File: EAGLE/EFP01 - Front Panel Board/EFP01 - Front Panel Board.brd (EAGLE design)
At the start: 100 x 86.6 mm, 109 parts, among them J20 Intel EDISON, J21 PWRBUTTON, J22 SERIAL CONS., J23 B14B-PH, J3 USB-A, J4 101-00581-59, J9 ESTOP, Q2 25MHz, U10 FT231XS-R, U11 74LVC1T45, U12 74LVC1T45, U13 74LVC1T45, U14 74LVC1T45, U15 74LVC1T45, U16 TXS0206-29, U17 74LVC, U18 MIC2026-1YM, U19 MIC2026-1YM, U20 74LVC, U21 74LVC1T45, U22 74LVC1T45, U3 93LC66A, U4 LAN9514, U9 SP3485

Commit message: Finalized schematics (minus potential LDO regulator) for all boards. Layout partially done for EFD01
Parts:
- removed C36: 220uF, TinWhiskers:C-SMD-10MM
- removed C50: 470uF, TinWhiskers:C-SMD-10MM
- removed FID4, FID5, FID6: FIDUCIAL, FirePick:FIDUCIAL
- removed J21: PWRBUTTON, TinWhiskers:CON-HDR-2POS-MALE
- removed J22: SERIAL CONS., TinWhiskers:CON-HDR-4POS-MALE
- removed J23: B14B-PH, TinWhiskers:CONN-JST-PH-2.0MM-14P-VRT
- removed J9: ESTOP, TinWhiskers:CON-HDR-2POS-MALE
- removed L2: 100uH, TinWhiskers:L-SMD-12.5MM
- added C1: 220uF, TinWhiskers:C-SMD-6.3MM
- added C3: 470uF, TinWhiskers:C-SMD-6.3MM
- added J1: PWRBTN, TinWhiskers:CONN-JST-PH-2.0MM-4P-SMT-RA
- added J16, J17, J6: S8B-PH-SM4, TinWhiskers:CONN-JST-PH-2.0MM-8P-SMT-RA
- added J18: S6B-PH-SM4, TinWhiskers:CONN-JST-PH-2.0MM-6P-SMT-RA
- added J2: ESTOP, TinWhiskers:CONN-JST-PH-2.0MM-2P-SMT-RA
- added J5: LCD, TinWhiskers:CON-HDR-34POS(2R)-MALE
- added J7: USB-B, TinWhiskers:USB-B(SMT)-VERT-1734517
- added L1: 100uH, TinWhiskers:2020
- added R1: 4.7K, TinWhiskers:R0603
- added R2: 10K, TinWhiskers:R0603
- added R3: ORNG, TinWhiskers:R0603
- added TB1: DCIN, TinWhiskers:TBLOCK-3-5MM-OSTTH030160
- added U1, U2, U23, U24, U25, U26, U27, U28, U30, U5, U6, U7, U8: 74LVC1T45, TinWhiskers:SOT-363
- J3: value USB-A -> USB-A(2.0); device TinWhiskers:CON-HDR-4POS-MALE -> TinWhiskers:USB-A-THRU-VERT-2.0
- U17, U20: value 74LVC -> OR
- moved J3 293.8 mm to (-11.4, -223.1), turned to 0 degrees
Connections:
- removed net ESTOP_OE: J9.2
- new net !ENBL_MOD: J16.2, J17.2, J18.2, J6.2
- new net +24V: J16.1, J17.1, J18.1, J6.1, R3.2, TB1.1
- new net 74DIR: J20.25, U30.3
- new net 74DIRO: U1.5, U2.5, U23.5, U24.5, U25.5, U26.5, U27.5, U28.5, U30.4, U5.5, U6.5, U7.5, U8.5
- new net D0O: J20.52, U24.4
- new net D1O: J20.54, U23.4
- new net D2O: J20.50, U7.4
- new net D3O: J20.56, U8.4
- new net D4O: J20.24, U6.4
- new net D5O: J20.26, U5.4
- new net D6O: J20.28, U1.4
- new net D7O: J20.30, U2.4
- new net ESTOPIN: J2.1, R2.1
- new net LCD_BL: J5.23
- new net LCD_CLK: J5.34
- new net LCD_D10: J5.16
- new net LCD_D11: J5.17
- new net LCD_D12: J5.18
- new net LCD_D13: J5.19
- new net LCD_D14: J5.20
- new net LCD_D15: J5.21
- new net LCD_D8: J5.14
- new net LCD_D9: J5.15
- new net LCD_FCS: J5.32
- new net LCD_MISO: J5.29
- new net LCD_MOSI: J5.30
- new net LCD_PEN: J5.31
- new net LCD_RST: J5.5
- new net LCD_SDCS: J5.22
- new net LCD_TCS: J5.33
- new net LCSO: J20.39, U25.4
- new net LRDO: J20.37, U27.4
- new net LRSO: J20.34, U28.4
- new net LWRO: J20.32, U26.4
- new net N$10: J2.2, R1.2
- new net NC: J5.28
- new net VDD: J5.24, J5.25
- net !PWRBTN: now also J1.1; no longer J21.1
- net +1V8: now also U1.1, U2.6, U23.1, U24.1, U25.6, U26.6, U27.6, U28.6, U30.6, U5.1, U6.1, U7.1, U8.6
- net +3V3: now also C3.POS, L1.2, R2.2, U1.6, U2.1, U23.6, U24.6, U25.1, U26.1, U27.1, U28.1, U30.1, U5.6, U6.6, U7.6, U8.1; no longer C50.POS, J23.1, L2.P$2
- net +5V: now also C1.POS, J18.6, J6.6, TB1.2; no longer C36.POS
- net A: now also J16.4, J17.4, J18.4, J6.4
- net B: now also J16.5, J17.5, J18.5, J6.5
- net DM: now also J7.3; no longer J22.3
- net DP: now also J7.2; no longer J22.2
- net EE_D+: now also J16.7
- net EE_D-: now also J16.8
- net GND: now also C1.NEG, C3.NEG, J1.2, J1.4, J16.3, J17.3, J18.3, J5.26, J5.27, J6.3, J7.4, R1.1, TB1.3, U1.2, U2.2, U23.2, U24.2, U25.2, U26.2, U27.2, U28.2, U30.2, U30.5, U5.2, U6.2, U7.2, U8.2; no longer C36.NEG, C50.NEG, J21.2, J22.4, J23.2
- net LCD_CS: now also J5.1, U25.3; no longer J20.39, J23.11
- net LCD_D0: now also J5.6, U24.3; no longer J20.52, J23.3
- net LCD_D1: now also J5.7, U23.3; no longer J20.54, J23.4
- net LCD_D2: now also J5.8, U7.3; no longer J20.50, J23.5
- net LCD_D3: now also J5.9, U8.3; no longer J20.56, J23.6
- net LCD_D4: now also J5.10, U6.3; no longer J20.24, J23.7
- net LCD_D5: now also J5.11, U5.3; no longer J20.26, J23.8
- net LCD_D6: now also J5.12, U1.3; no longer J20.28, J23.9
- net LCD_D7: now also J5.13, U2.3; no longer J20.30, J23.10
- net LCD_RD: now also J5.4, U27.3; no longer J20.37, J23.14
- net LCD_RS: now also J5.2, U28.3; no longer J20.34, J23.12
- net LCD_WR: now also J5.3, U26.3; no longer J20.32, J23.13
- net N$16: now also L1.1; no longer L2.P$1
- net N$2: now also J7.1; no longer J22.1
- net N$5: now also J1.3, R3.1; no longer J9.1
- net PWR1: now also J16.6
- net PWR2: now also J17.6
- net ULC_D+: now also J17.7
- net ULC_D-: now also J17.8
- net USBMCU+: now also J6.7
- net USBMCU-: now also J6.8

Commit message: Routed all boards. EFP01 has a serious problem with spacing. Even on minimum allowable there are 300 DRC errors.
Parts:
- removed C1: 220uF, TinWhiskers:C-SMD-6.3MM
- removed C33, C34, C35: 0.1uF, TinWhiskers:C0603
- removed C51: 0.47uF, TinWhiskers:C0603
- removed D15: SJPB-H6, TinWhiskers:DIO-SM2
- removed J4: 101-00581-59, TinWhiskers:MICRO-SD-SOCKET-AMPH
- removed L1: 100uH, TinWhiskers:2020
- removed R17, R23: 10.5K, TinWhiskers:R0603
- removed U16: TXS0206-29, TinWhiskers:20-XFBGA
- removed VR2: SI-8033JD, TinWhiskers:TO263-5
- added C4: 10uF, TinWhiskers:C-SMD-6.3MM
- added VR1: LMS8117AMP-3.3/NOPB, TinWhiskers:SOT-223
- C3: value 470uF -> 10uF
- J5: device TinWhiskers:CON-HDR-34POS(2R)-MALE -> TinWhiskers:LCD-34P-3.2IN
- moved J3 318.3 mm to (197.1, 17.3), turned to 90 degrees
- moved U30 303.1 mm to (163.4, 67.1), flipped to the bottom, turned to 270 degrees
- moved J7 301.0 mm to (132.6, 62.0), flipped to the bottom
- moved J6 237.6 mm to (127.2, 7.98), flipped to the bottom, turned to 180 degrees
- moved C3 229.1 mm to (29.7, 12.9), flipped to the bottom, turned to 180 degrees
- moved U28 198.1 mm to (50.6, 14.8), flipped to the bottom, turned to 270 degrees
- moved U27 195.3 mm to (50.7, 17.8), flipped to the bottom, turned to 270 degrees
- moved U26 193.1 mm to (64.5, 17.3), flipped to the bottom
- moved U25 184.0 mm to (64.5, 13.7), flipped to the bottom
- moved U23 181.9 mm to (64.6, 23.3), flipped to the bottom
- moved U24 181.2 mm to (50.7, 21.1), flipped to the bottom, turned to 270 degrees
- moved U8 179.5 mm to (64.5, 26.7), flipped to the bottom
- moved U7 167.1 mm to (50.7, 24.3), flipped to the bottom, turned to 270 degrees
- moved J2 166.4 mm to (69.0, 61.6), flipped to the bottom
- moved U5 166.1 mm to (64.5, 30.2), flipped to the bottom
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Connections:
- removed net CLKA: J20.58, U16.D2
- removed net CLKB: J4.5, U16.D3
- removed net CLKF: J20.44, U16.E2
- removed net CMD: J4.3
- removed net CMDA: J20.62, U16.C1
- removed net CMDB: U16.C4
- removed net DAT0A: J20.66, U16.D1
- removed net DAT0B: J4.7, U16.D4
- removed net DAT1A: J20.70, U16.E1
- removed net DAT1B: J4.8, U16.E4
- removed net DAT2: J4.1
- removed net DAT2A: J20.64, U16.A1
- removed net DAT2B: U16.A4
- removed net DAT3: J4.2
- removed net DAT3A: J20.68, U16.B1
- removed net DAT3B: U16.B4
- removed net EN: R17.1, U16.E3
- removed net N$16: D15.POS, L1.1, VR2.2
- removed net N$17: C51.2, VR2.5
- removed net SD_CD: J20.60, J4.CD, R23.1, U16.A3
- removed net VCCB: C34.2, J4.4, U16.B3
- new net RESET: U10.14
- net !RXLED: now also U10.10
- net !TXLED: now also U10.17
- net +1V8: no longer C35.2, R17.2, R23.2, U16.A2
- net +3V3: now also C4.POS, U10.3, VR1.2; no longer C3.POS, C33.2, L1.2, U16.B2, VR2.4
- net +5V: now also C3.POS, VR1.3; no longer C1.POS, VR2.1
- net DM: now also U10.12
- net DP: now also U10.11
- net GND: now also C4.NEG, RJ1.8, U10.16, U10.6, VR1.1, VR1.P$1; no longer C1.NEG, C33.1, C34.1, C35.1, C51.1, D15.NEG, J4.6, J4.GND, J4.GND2, J4.NC, U16.C2, U16.C3, VR2.3, VR2.GND
- net N$1: now also U10.13
- net RXD: now also U10.4
- net TXDO: now also U10.20
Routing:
- net +3V3: track 0.00 -> 583.4 mm, vias 0 -> 34
- net +5V: track 0.00 -> 323.3 mm, vias 0 -> 5
- net GND: track 0.00 -> 308.2 mm, vias 0 -> 88
- net +1V8: track 0.00 -> 284.1 mm, vias 0 -> 26
- net 74DIRO: track 0.00 -> 229.8 mm, vias 0 -> 14
- net LRSO: track 0.00 -> 198.0 mm, vias 0 -> 8
- net D0O: track 0.00 -> 182.0 mm, vias 0 -> 4
- net LRDO: track 0.00 -> 180.1 mm, vias 0 -> 2
- net D2O: track 0.00 -> 174.3 mm, vias 0 -> 4
- net LCSO: track 0.00 -> 169.4 mm, vias 0 -> 6
- net B: track 0.00 -> 163.0 mm, vias 0 -> 7
- net D1O: track 0.00 -> 162.5 mm, vias 0 -> 2
- net D4O: track 0.00 -> 161.9 mm, vias 0 -> 4
- net D3O: track 0.00 -> 158.6 mm, vias 0 -> 2
- net LWRO: track 0.00 -> 158.6 mm, vias 0 -> 2
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- added copper zone on layer 15, net +24V
- added copper zone on layer 2, net GND
- removed copper zone on layer 1, net GND
- removed copper zone on layer 16, net GND
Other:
- board size 100 x 86.6 mm -> 200 x 69.6 mm
- board text removed: "ENCODER"
- board text removed: "ENDSTOP"
- board text removed: "MOT"
- board text removed: "RXD"
- board text removed: "X AXIS"
- board text removed: "Y AXIS"

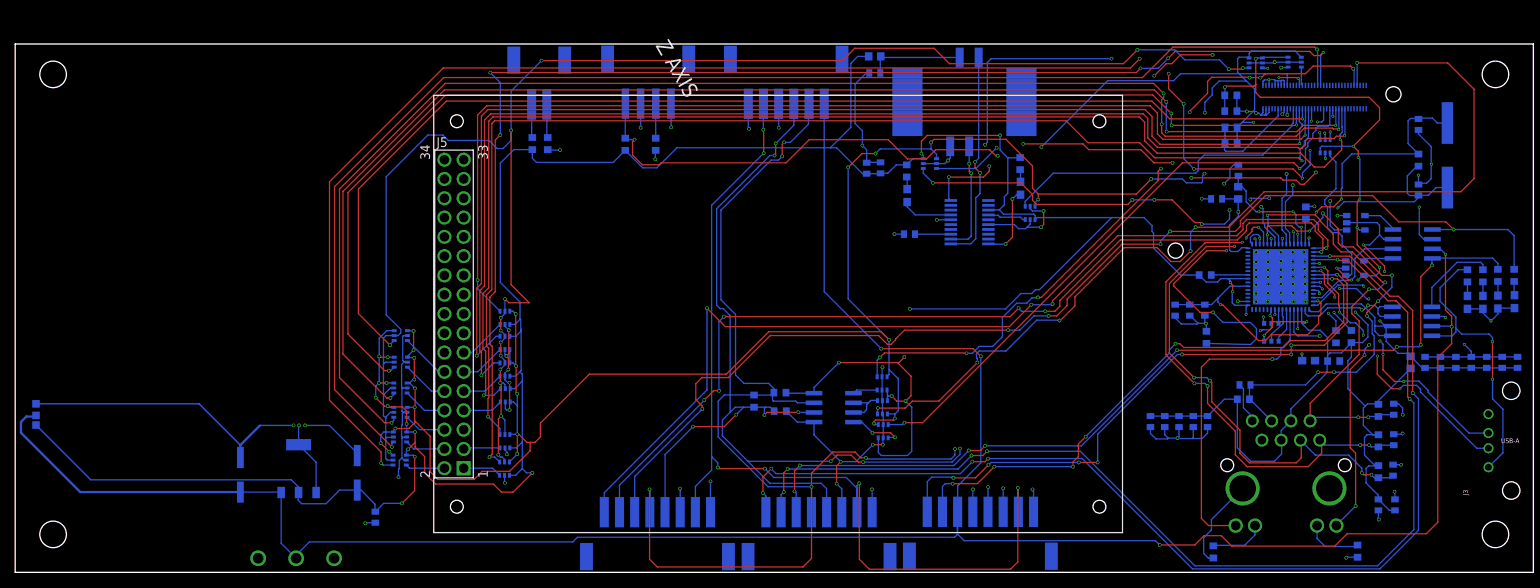
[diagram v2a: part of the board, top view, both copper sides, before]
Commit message: Completed boards. Please look at airwires connecting thermal pads to GND vias. They shouldn't be present due to the vias.
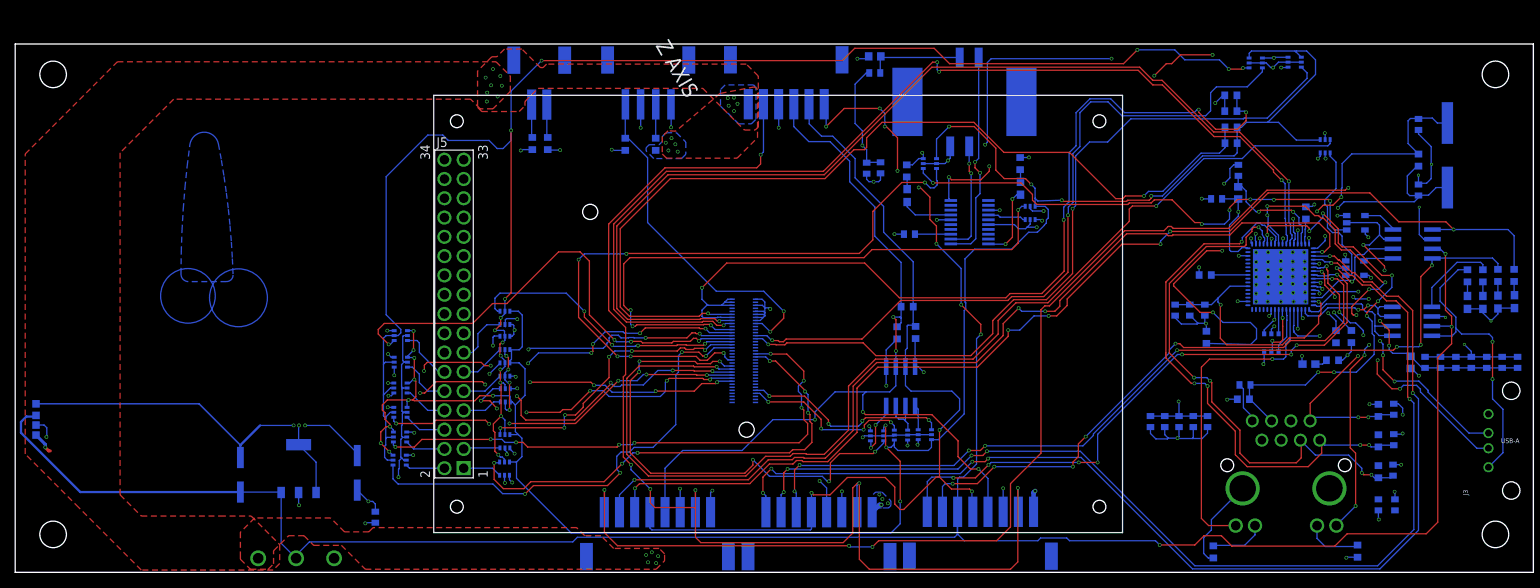
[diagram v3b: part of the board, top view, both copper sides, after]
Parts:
- added TP3: +5V, TinWhiskers:TESTPAD
- J1: device TinWhiskers:CONN-JST-PH-2.0MM-4P-SMT-RA -> TinWhiskers:CON-JST-PH-2.0MM-4P-SMT-RA
- J2: device TinWhiskers:CONN-JST-PH-2.0MM-2P-SMT-RA -> TinWhiskers:CON-JST-PH-2.0MM-2P-SMT-RA
- moved J20 82.3 mm to (96.0, 29.2), turned to 270 degrees
- moved R51 23.7 mm to (117.5, 35.0), turned to 180 degrees
- moved R49 19.6 mm to (118.6, 31.6), turned to 270 degrees
- moved R50 18.5 mm to (116.2, 31.5), turned to 90 degrees
- moved U9 9.24 mm to (116.6, 24.5), turned to 90 degrees
- moved U15 8.80 mm to (119.8, 18.1), turned to 90 degrees
- moved U14 4.40 mm to (116.7, 18.1), turned to 90 degrees
- moved U3 1.37 mm to (165.5, 30.3)
- moved U13 1.02 mm to (113.5, 18.0), turned to 270 degrees
- moved LED11 0.46 mm to (170.4, 27.4)
- moved R10 0.18 mm to (173.5, 27.9), turned to 180 degrees
- moved J1 0.10 mm to (83.4, 61.6)
- moved J18 0.05 mm to (101.6, 61.7)
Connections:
- net +24V: now also TP3.PAD
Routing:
- net +3V3: track 583.4 -> 76.5 mm, vias 34 -> 41
- net EEEN: track 4.47 -> 142.7 mm
- net LRSO: track 198.0 -> 62.8 mm, vias 8 -> 4
- net D0O: track 182.0 -> 48.3 mm, vias 4 -> 6
- net D3O: track 158.6 -> 35.6 mm, vias 2 -> 5
- net USBDM0: track 18.4 -> 140.9 mm, vias 2 -> 4
- net D1O: track 162.5 -> 40.7 mm, vias 2 -> 6
- net D2O: track 174.3 -> 53.5 mm, vias 4 -> 7
- net USBDP0: track 19.1 -> 138.9 mm
- net LWRO: track 158.6 -> 39.2 mm, vias 2 -> 6
- net D5O: track 152.4 -> 35.6 mm, vias 2 -> 4
- net D4O: track 161.9 -> 49.9 mm, vias 4 -> 8
- net N$21: track 8.97 -> 118.7 mm, vias 2 -> 4
- net N$19: track 13.0 -> 121.6 mm, vias 0 -> 2
- net LRDO: track 180.1 -> 73.1 mm, vias 2 -> 8
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- added copper zone on layer 1, net +24V
- added copper zone on layer 16, net +24V
- added copper zone on layer 15, net +3V3
- added copper zone on layer 16, net N$4

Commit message: Updated all boards to include changes for production
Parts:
- added C1, C10, C15, C16, C17, C27, C28, C29, C33, C34, C35, C36, C37, C38, C39, C40, C41, C42, C43, C44, C45, C46, C47, C48, C49, C5, C6, C7, C8, C9: 0.1uF, TinWhiskers:C0603
- added LOGO1, LOGO2: LOGO-FIREPICKLARGE, FirePick:LOGO-FIREPICK
- J16, J17, J6: device TinWhiskers:CONN-JST-PH-2.0MM-8P-SMT-RA -> TinWhiskers:CON-JST-PH-2.0MM-8P-SMT-VRT
- J18: device TinWhiskers:CONN-JST-PH-2.0MM-6P-SMT-RA -> TinWhiskers:CON-JST-PH-2.00MM-6P-SMT-VRT
- moved C11 16.8 mm to (168.8, 54.1), turned to 0 degrees
- moved Q2 16.1 mm to (172.8, 57.9), turned to 180 degrees
- moved R11 11.4 mm to (173.5, 54.1), turned to 180 degrees
- moved C12 8.30 mm to (177.4, 54.1), turned to 180 degrees
- moved C4 6.84 mm to (39.9, 17.6)
- moved VR1 6.65 mm to (32.5, 18.2)
- moved C3 6.61 mm to (24.9, 17.4)
- moved U22 6.61 mm to (174.0, 62.6), turned to 90 degrees
- moved U21 5.44 mm to (120.8, 48.4)
- moved U30 5.04 mm to (163.7, 62.1)
- moved C60 5.04 mm to (114.2, 48.3)
- moved C77 5.04 mm to (118.1, 39.5)
- moved C78 5.04 mm to (113.5, 60.8)
- moved J1 5.04 mm to (83.6, 56.6)
- moved LED9 5.04 mm to (132.7, 45.6)
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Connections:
- net +3V3: now also C1.2, C10.2, C15.2, C16.2, C17.2, C27.2, C28.2, C29.2, C33.2, C34.2, C35.2, C36.2, C37.2, C38.2, C39.2, C40.2, C41.2, C42.2, C43.2, C44.2, C45.2, C46.2, C47.2, C48.2, C49.2, C5.2, C6.2, C7.2, C8.2, C9.2, VR1.P$1; no longer VR1.2
- net GND: now also C1.1, C10.1, C15.1, C16.1, C17.1, C27.1, C28.1, C29.1, C33.1, C34.1, C35.1, C36.1, C37.1, C38.1, C39.1, C40.1, C41.1, C42.1, C43.1, C44.1, C45.1, C46.1, C47.1, C48.1, C49.1, C5.1, C6.1, C7.1, C8.1, C9.1; no longer VR1.P$1
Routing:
- net +3V3: track 76.5 -> 198.1 mm, vias 41 -> 60
- net GND: track 292.0 -> 349.4 mm, vias 87 -> 107
- net EEENO: track 19.7 -> 53.4 mm
- net XO: track 36.7 -> 25.7 mm, vias 3 -> 2
- net +1V8: track 282.4 -> 272.5 mm, vias 16 -> 23
- net N$21: track 118.7 -> 109.4 mm
- net B: track 123.3 -> 131.2 mm, vias 3 -> 5
- net +24V: track 11.6 -> 4.66 mm, vias 30 -> 36
- net TXD: track 100.6 -> 94.4 mm
- net !PWRBTN: track 45.8 -> 40.7 mm
- net 74DIRO: track 227.7 -> 223.2 mm
- net USBA_D-: track 39.0 -> 42.9 mm, vias 5 -> 6
- net USBA_D+: track 35.3 -> 39.3 mm, vias 5 -> 6
- net RD-: track 61.2 -> 65.1 mm
- net !ENBL_MOD: track 163.2 -> 167.1 mm, vias 6 -> 7
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- removed copper zone on layer 16, net N$4
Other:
- board size 200 x 69.6 mm -> 200 x 65 mm
- board text added: "E-STOP"
- board text added: "EMC03"
- board text added: "END EFFECTOR"
- board text added: "ETHERNET"
- board text added: "LCD"
- board text added: "MOD TOOL"
- board text added: "PWR"
- board text added: "PWR BTN"
- board text added: "SBC"
- board text added: "UP-LOOK CAM"
- board text added: "USB-B"
- board text removed: "Z AXIS"

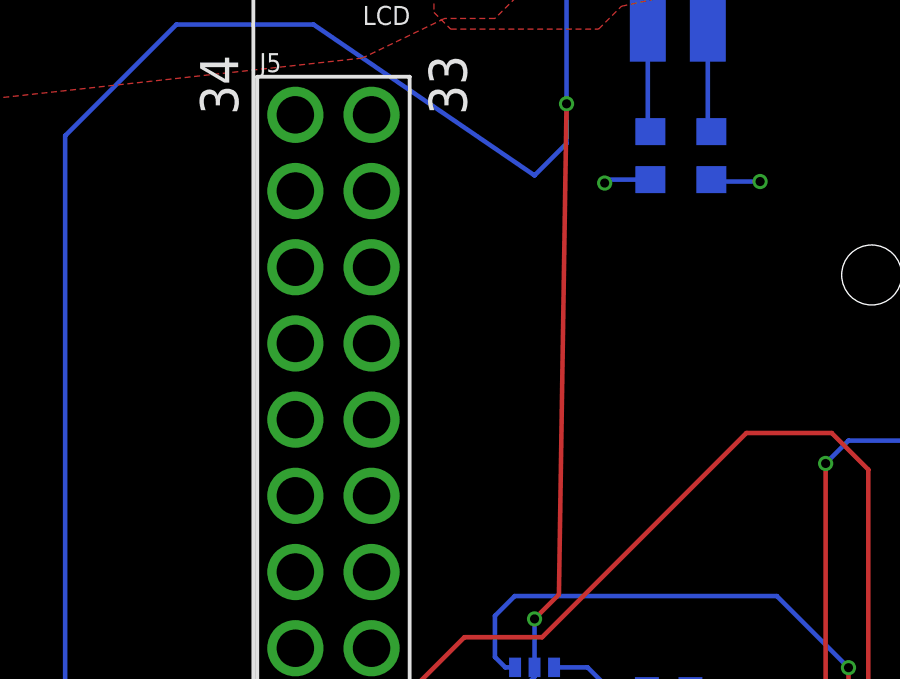
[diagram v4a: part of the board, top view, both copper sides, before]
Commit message: Added +3V3 line for LCD, DXF for Will
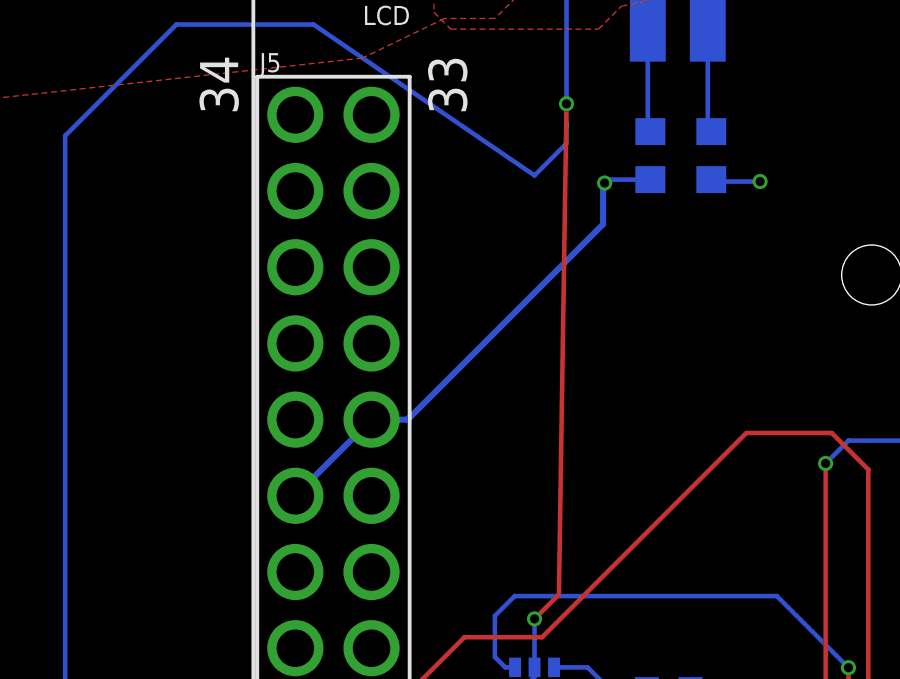
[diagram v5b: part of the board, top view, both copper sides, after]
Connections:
- removed net VDD: J5.24, J5.25
- net +3V3: now also J5.24, J5.25
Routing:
- net +3V3: track 198.1 -> 213.5 mm
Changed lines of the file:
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@@
 <layer number="25" name="tNames" color="7" fill="1" visible="yes" active="yes"/>
 <layer number="26" name="bNames" color="7" fill="1" visible="yes" active="yes"/>
-<layer number="27" name="tValues" color="7" fill="1" visible="no" active="yes"/>
-<layer number="28" name="bValues" color="7" fill="1" visible="no" active="yes"/>
+<layer number="27" name="tValues" color="7" fill="1" visible="yes" active="yes"/>
+<layer number="28" name="bValues" color="7" fill="1" visible="yes" active="yes"/>
 <layer number="29" name="tStop" color="7" fill="3" visible="yes" active="yes"/>
 <layer number="30" name="bStop" color="7" fill="6" visible="yes" active="yes"/>
@@
 <layer number="42" name="bRestrict" color="1" fill="10" visible="yes" active="yes"/>
 <layer number="43" name="vRestrict" color="2" fill="10" visible="yes" active="yes"/>
-<layer number="44" name="Drills" color="7" fill="1" visible="no" active="yes"/>
+<layer number="44" name="Drills" color="7" fill="1" visible="yes" active="yes"/>
 <layer number="45" name="Holes" color="7" fill="1" visible="yes" active="yes"/>
 <layer number="46" name="Milling" color="3" fill="1" visible="yes" active="yes"/>
@@
 <layer number="49" name="Reference" color="7" fill="1" visible="yes" active="yes"/>
 <layer number="50" name="dxf" color="7" fill="1" visible="no" active="no"/>
-<layer number="51" name="tDocu" color="7" fill="1" visible="no" active="yes"/>
+<layer number="51" name="tDocu" color="7" fill="1" visible="yes" active="yes"/>
 <layer number="52" name="bDocu" color="7" fill="1" visible="yes" active="yes"/>
 <layer number="53" name="tGND_GNDA" color="7" fill="9" visible="no" active="no"/>
@@
 <wire x1="41.0464" y1="22.8092" x2="33.934" y2="22.8092" width="0.3048" layer="16"/>
 <wire x1="33.934" y1="22.8092" x2="32.512" y2="21.3872" width="0.3048" layer="16"/>
+<contactref element="J5" pad="24"/>
+<contactref element="J5" pad="25"/>
+<wire x1="56.543" y1="40.12" x2="59.083" y2="42.66" width="0.2032" layer="16"/>
+<wire x1="59.083" y1="42.66" x2="60.2876" y2="42.66" width="0.2032" layer="16"/>
+<wire x1="60.2876" y1="42.66" x2="66.802" y2="49.1744" width="0.2032" layer="16"/>
+<wire x1="66.802" y1="49.1744" x2="66.802" y2="50.4952" width="0.2032" layer="16"/>
+<wire x1="66.802" y1="50.4952" x2="66.8528" y2="50.546" width="0.2032" layer="16"/>
 </signal>
 <signal name="TD+">
@@
 <contactref element="J5" pad="23"/>
 </signal>
-<signal name="VDD">
-<contactref element="J5" pad="25"/>
-<contactref element="J5" pad="24"/>
-<wire x1="56.543" y1="40.12" x2="59.083" y2="42.66" width="0" layer="19" extent="1-1"/>
-</signal>
 <signal name="LCD_MISO">
